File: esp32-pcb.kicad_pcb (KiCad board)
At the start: 2 copper layers, 25.2 x 59.4 mm, 47 parts, among them J1 Conn_01x15_Male, J2 Conn_01x15_Male, Q1 TSM2323CX, Q2 BSS138Q-7-F, Q3 MMBT3904, Q4 MMBT3904, SW1 RESET, SW2 USER, SW3 SW_DIP_x04, U1 TLV75533, U2 ESP32-WROOM-32, U3 CP2102N-A01-GQFN24

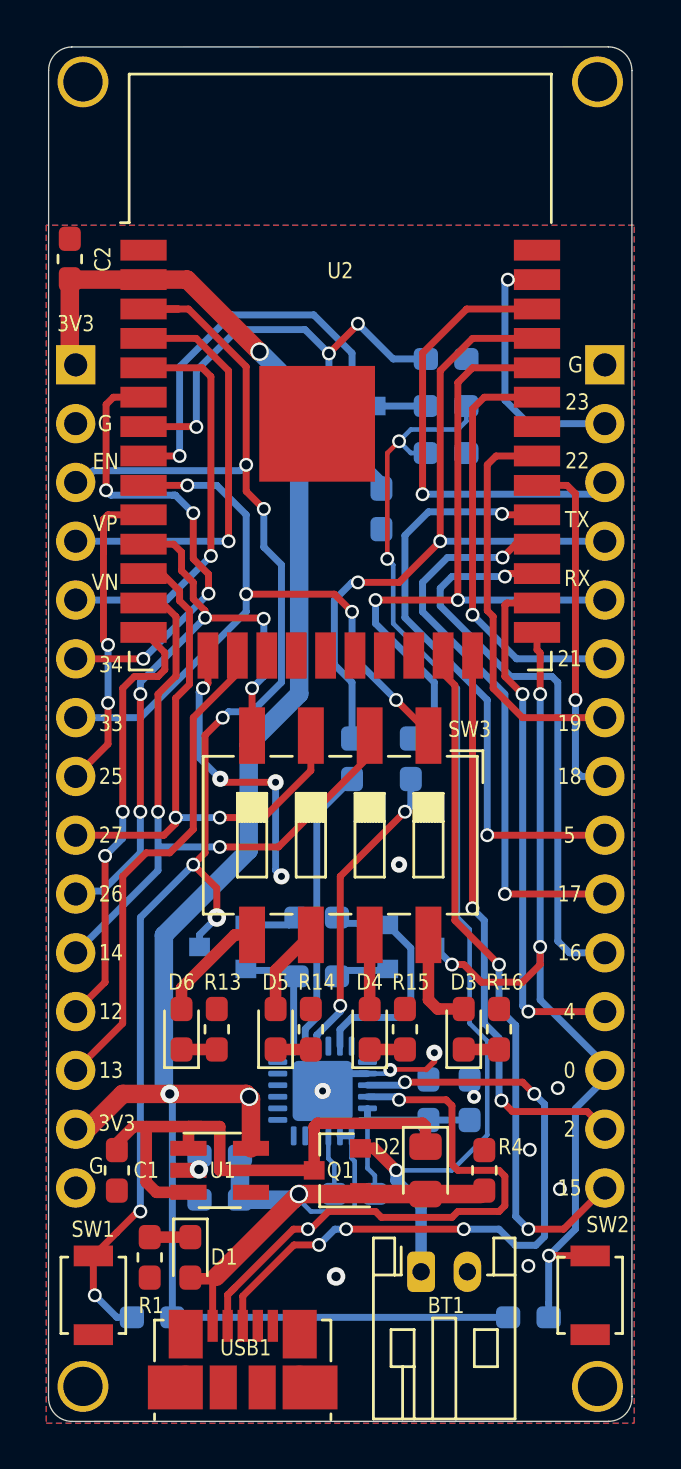
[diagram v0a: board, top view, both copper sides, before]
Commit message: Make battery power line 0.7mm
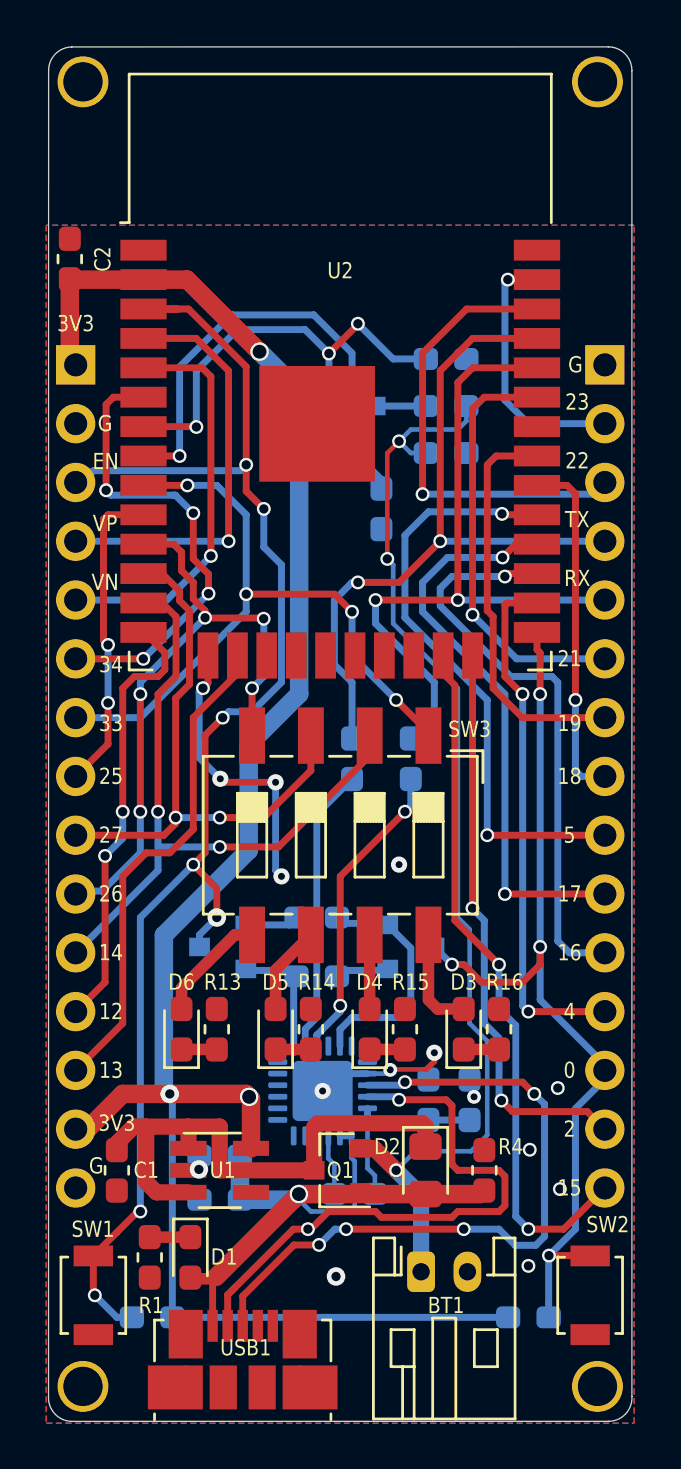
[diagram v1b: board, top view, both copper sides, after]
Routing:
- net Net-(C1-Pad1): track 24.6 -> 24.0 mm
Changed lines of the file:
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@@
     (thickness 1.6)
     (drawings 3056)
-    (tracks 586)
+    (tracks 585)
     (zones 0)
     (modules 47)
@@
   (page A4)
   (layers
-    (0 F.Cu signal hide)
+    (0 F.Cu signal)
     (31 B.Cu signal)
     (32 B.Adhes user)
@@
   (via (at 139.192 104.14) (size 0.7) (drill 0.3) (layers F.Cu B.Cu) (net 1))
   (via (at 144.272 103.632) (size 0.7) (drill 0.3) (layers F.Cu B.Cu) (net 1))
-  (segment (start 142.605 115.89) (end 143.195 115.89) (width 0.5) (layer F.Cu) (net 2) (status 10))
-  (via (at 144.145 116.84) (size 0.6) (drill 0.4) (layers F.Cu B.Cu) (net 2))
-  (segment (start 143.195 115.89) (end 144.145 116.84) (width 0.5) (layer F.Cu) (net 2))
   (via (at 144.272 85.344) (size 0.6) (drill 0.4) (layers F.Cu B.Cu) (net 2))
-  (segment (start 146.558 116.84) (end 144.145 116.84) (width 0.2) (layer B.Cu) (net 2))
-  (segment (start 148.082 115.316) (end 146.558 116.84) (width 0.2) (layer B.Cu) (net 2))
-  (segment (start 148.082 111.252) (end 148.082 115.316) (width 0.2) (layer B.Cu) (net 2))
-  (segment (start 147.32 110.49) (end 148.082 111.252) (width 0.2) (layer B.Cu) (net 2))
-  (segment (start 147.32 106.426) (end 147.32 110.49) (width 0.2) (layer B.Cu) (net 2))
-  (segment (start 146.812 96.012) (end 146.812 105.918) (width 0.2) (layer B.Cu) (net 2))
-  (segment (start 144.018 93.218) (end 146.812 96.012) (width 0.2) (layer B.Cu) (net 2))
-  (segment (start 144.018 90.678) (end 144.018 93.218) (width 0.2) (layer B.Cu) (net 2))
   (via (at 143.764 90.424) (size 0.6) (drill 0.4) (layers F.Cu B.Cu) (net 2))
-  (segment (start 146.812 105.918) (end 147.32 106.426) (width 0.2) (layer B.Cu) (net 2))
-  (segment (start 143.764 90.424) (end 144.018 90.678) (width 0.2) (layer B.Cu) (net 2))
   (segment (start 143.764 85.852) (end 144.272 85.344) (width 0.2) (layer F.Cu) (net 2))
   (segment (start 143.764 90.424) (end 143.764 85.852) (width 0.2) (layer F.Cu) (net 2))
@@
   (segment (start 144.78 85.852) (end 144.272 85.344) (width 0.2) (layer B.Cu) (net 2))
   (segment (start 145.429 85.852) (end 144.78 85.852) (width 0.2) (layer B.Cu) (net 2) (status 10))
-  (segment (start 144.145 116.84) (end 144.145 117.2845) (width 0.5) (layer B.Cu) (net 2))
-  (segment (start 145.2245 118.364) (end 145.2245 121.2215) (width 0.5) (layer B.Cu) (net 2) (status 20))
-  (segment (start 144.145 117.2845) (end 145.2245 118.364) (width 0.5) (layer B.Cu) (net 2))
+  (segment (start 145.2245 117.9195) (end 145.2245 121.2215) (width 0.7) (layer B.Cu) (net 2))
+  (segment (start 144.145 116.84) (end 145.2245 117.9195) (width 0.7) (layer B.Cu) (net 2))
+  (segment (start 144.145 116.84) (end 143.195 115.89) (width 0.7) (layer F.Cu) (net 2))
+  (via (at 144.145 116.84) (size 0.6) (drill 0.4) (layers F.Cu B.Cu) (net 2))
+  (segment (start 143.195 115.89) (end 142.605 115.89) (width 0.7) (layer F.Cu) (net 2))
+  (segment (start 146.812 96.012) (end 144.018 93.218) (width 0.2) (layer B.Cu) (net 2))
+  (segment (start 146.812 105.918) (end 146.812 96.012) (width 0.2) (layer B.Cu) (net 2))
+  (segment (start 147.32 106.426) (end 146.812 105.918) (width 0.2) (layer B.Cu) (net 2))
+  (segment (start 144.9705 116.0145) (end 147.3835 116.0145) (width 0.2) (layer B.Cu) (net 2))
+  (segment (start 144.018 93.218) (end 144.018 90.678) (width 0.2) (layer B.Cu) (net 2))
+  (segment (start 147.32 110.49) (end 147.32 106.426) (width 0.2) (layer B.Cu) (net 2))
+  (segment (start 144.145 116.84) (end 144.9705 116.0145) (width 0.2) (layer B.Cu) (net 2))
+  (segment (start 147.3835 116.0145) (end 148.082 115.316) (width 0.2) (layer B.Cu) (net 2))
+  (segment (start 148.082 115.316) (end 148.082 111.252) (width 0.2) (layer B.Cu) (net 2))
+  (segment (start 144.018 90.678) (end 143.764 90.424) (width 0.2) (layer B.Cu) (net 2))
+  (segment (start 148.082 111.252) (end 147.32 110.49) (width 0.2) (layer B.Cu) (net 2))
   (segment (start 130.062 78.359) (end 130.048 78.345) (width 0.8) (layer F.Cu) (net 3) (status 30))
   (segment (start 133.232 78.359) (end 130.062 78.359) (width 0.8) (layer F.Cu) (net 3) (status 30))
@@
   (segment (start 150.114 113.538) (end 150.5585 113.9825) (width 0.3) (layer B.Cu) (net 70))
   (segment (start 150.5585 113.9825) (end 150.5585 119.6975) (width 0.3) (layer B.Cu) (net 70))
-  (segment (start 140.605 114.951) (end 140.605 116.84) (width 0.5) (layer F.Cu) (net 73) (status 20))
+  (segment (start 140.605 114.951) (end 140.605 116.84) (width 0.7) (layer F.Cu) (net 73) (status 20))
   (segment (start 140.748 114.808) (end 140.605 114.951) (width 0.5) (layer F.Cu) (net 73))
-  (segment (start 145.288 114.808) (end 140.748 114.808) (width 0.5) (layer F.Cu) (net 73))
-  (segment (start 145.415 115.815) (end 145.415 114.935) (width 0.5) (layer F.Cu) (net 73) (status 10))
-  (segment (start 145.415 114.935) (end 145.288 114.808) (width 0.5) (layer F.Cu) (net 73))
-  (segment (start 132.8 114.95) (end 135.75 114.95) (width 0.5) (layer F.Cu) (net 73))
+  (segment (start 145.288 114.808) (end 140.748 114.808) (width 0.7) (layer F.Cu) (net 73))
   (segment (start 132.08 115.965) (end 132.08 115.67) (width 0.5) (layer F.Cu) (net 73) (status 30))
-  (segment (start 132.08 115.67) (end 132.8 114.95) (width 0.5) (layer F.Cu) (net 73) (status 10))
-  (segment (start 136.525 116.84) (end 140.605 116.84) (width 0.5) (layer F.Cu) (net 73) (status 20))
-  (segment (start 136.525 114.95) (end 136.525 116.84) (width 0.5) (layer F.Cu) (net 73))
-  (segment (start 135.175 115.89) (end 135.175 114.95) (width 0.5) (layer F.Cu) (net 73) (status 10))
-  (segment (start 135.175 114.95) (end 136.525 114.95) (width 0.5) (layer F.Cu) (net 73))
-  (segment (start 133.35 117.348) (end 133.35 114.95) (width 0.5) (layer F.Cu) (net 73))
-  (segment (start 135.175 117.79) (end 133.792 117.79) (width 0.5) (layer F.Cu) (net 73) (status 10))
-  (segment (start 133.792 117.79) (end 133.35 117.348) (width 0.5) (layer F.Cu) (net 73))
+  (segment (start 132.08 115.67) (end 132.8 114.95) (width 0.7) (layer F.Cu) (net 73) (status 10))
+  (segment (start 136.525 116.84) (end 140.605 116.84) (width 0.7) (layer F.Cu) (net 73) (status 20))
+  (segment (start 136.525 114.95) (end 136.525 116.84) (width 0.7) (layer F.Cu) (net 73))
+  (segment (start 135.175 115.89) (end 135.175 114.95) (width 0.7) (layer F.Cu) (net 73) (status 10))
+  (segment (start 133.35 117.348) (end 133.35 114.95) (width 0.7) (layer F.Cu) (net 73))
+  (segment (start 135.175 117.79) (end 133.792 117.79) (width 0.7) (layer F.Cu) (net 73) (status 10))
+  (segment (start 133.792 117.79) (end 133.35 117.348) (width 0.7) (layer F.Cu) (net 73))
+  (segment (start 145.415 114.935) (end 145.288 114.808) (width 0.7) (layer F.Cu) (net 73))
+  (segment (start 145.415 115.815) (end 145.415 114.935) (width 0.7) (layer F.Cu) (net 73))
+  (segment (start 132.8 114.95) (end 136.525 114.95) (width 0.7) (layer F.Cu) (net 73))
   (zone (net 1) (net_name GND) (layer B.Cu) (hatch edge 0.508)
     (connect_pads yes (clearance 0.25))

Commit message: Added even more vias and aligned them so that they do not interfere with graphics
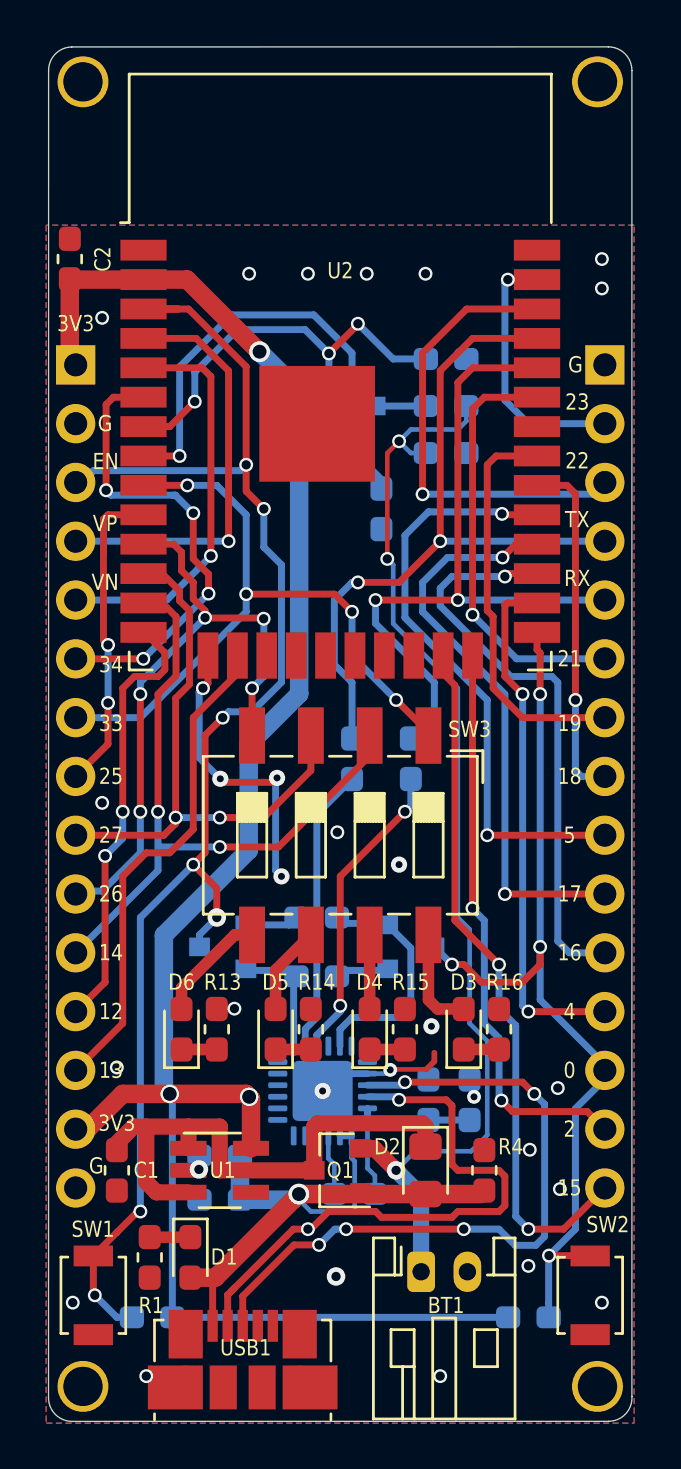
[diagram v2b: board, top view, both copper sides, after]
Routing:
- net 5V_USB: track 27.4 -> 28.4 mm
- net V_BAT_HALF: track 18.3 -> 17.6 mm
- net GND: vias 15 -> 30

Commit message: Adapted replacement of DOGE to DOGE32
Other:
- board text added: "DOGE32 v1.0"
- board text removed: "DOGE v1.0"
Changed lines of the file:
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@@
     (effects (font (size 0.75 0.75) (thickness 0.15)) (justify mirror))
   )
-  (gr_text "DOGE v1.0" (at 137.414 93.853) (layer B.SilkS)
+  (gr_text "DOGE32 v1.0" (at 137.414 93.853) (layer B.SilkS)
     (effects (font (size 1 1) (thickness 0.15)) (justify mirror))
   )
